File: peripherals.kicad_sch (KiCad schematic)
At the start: 36 parts, among them J10 SM04B-SRSS-TB, J11 U254-051T-4BH81-S2S, J3 UEXT, J8 XKTF-0803-0, Q1 BSS138, SW2 PROG_EN, U3 CH340C, U4 PCF8563T, Y1 32kHz

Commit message: Put resistor before switch to avoid parasitic powering of the board
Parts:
- R1: value 4.7K -> 1K
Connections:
- net USBTX: now also R1.2; no longer U3.2 (TXD)
- net at D1.1 (K): now also SW2.3 (C); no longer R1.2
- net at R1.1: now also U3.2 (TXD); no longer SW2.3 (C)
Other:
- moved on the sheet: R1
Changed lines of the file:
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@@
+    (stroke (width 0) (type default))
+  )
+  (wire (pts (xy 75.565 37.465) (xy 67.945 37.465))
     (stroke (width 0) (type default))
   )
@@
     (stroke (width 0) (type default))
   )
-  (wire (pts (xy 81.915 37.465) (xy 67.945 37.465))
+  (wire (pts (xy 81.915 37.465) (xy 80.645 37.465))
     (stroke (width 0) (type default))
   )
@@
     (stroke (width 0) (type default))
   )
-  (wire (pts (xy 43.18 40.005) (xy 40.64 40.005))
-    (stroke (width 0) (type default))
-  )
   (wire (pts (xy 119.38 53.975) (xy 111.76 53.975))
     (stroke (width 0) (type default))
@@
     (stroke (width 0) (type default))
   )
-  (wire (pts (xy 57.785 40.005) (xy 48.26 40.005))
+  (wire (pts (xy 40.64 40.005) (xy 57.785 40.005))
     (stroke (width 0) (type default))
   )
@@
     )
   )
-  (symbol (lib_id "Device:R_Small") (at 45.72 40.005 270) (unit 1)
+  (symbol (lib_id "Device:R_Small") (at 78.105 37.465 270) (unit 1)
     (in_bom yes) (on_board yes) (dnp no)
-    (property "Reference" "R1" (at 43.815 35.56 90)
+    (property "Reference" "R1" (at 76.2 33.02 90)
       (effects (font (size 1.27 1.27)) (justify left))
     )
-    (property "Value" "4.7K" (at 43.815 38.1 90)
+    (property "Value" "1K" (at 76.2 35.56 90)
       (effects (font (size 1.27 1.27)) (justify left))
     )
-    (property "Footprint" "Resistor_SMD:R_0402_1005Metric" (at 45.72 40.005 0)
-      (effects (font (size 1.27 1.27)) hide)
-    )
-    (property "Datasheet" "~" (at 45.72 40.005 0)
-      (effects (font (size 1.27 1.27)) hide)
-    )
+    (property "Footprint" "Resistor_SMD:R_0402_1005Metric" (at 78.105 37.465 0)
+      (effects (font (size 1.27 1.27)) hide)
+    )
+    (property "Datasheet" "~" (at 78.105 37.465 0)
+      (effects (font (size 1.27 1.27)) hide)
+    )

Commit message: Final touches
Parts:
- BT1: now not fitted
- renumbered C9 to C8, C10 to C9, D1 to D2, J3 to J11, J10 to J12, J11 to J9, R10 to R2, R12 to R3, R13 to R4, R14 to R5, R11 to R6, SW2 to SW3

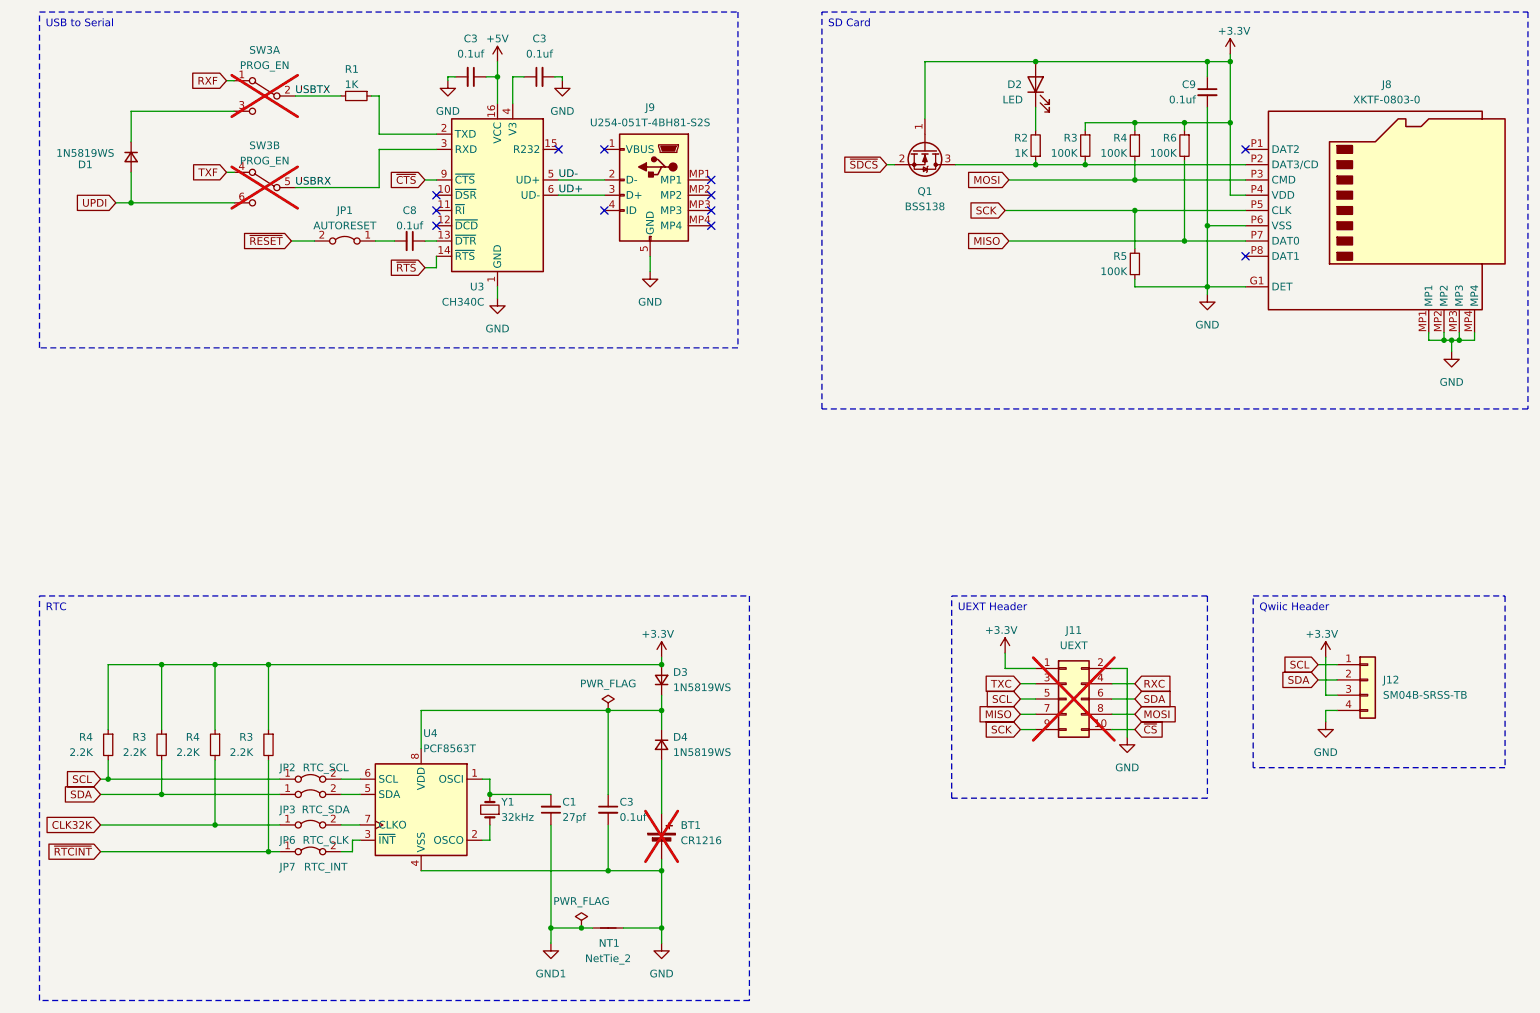
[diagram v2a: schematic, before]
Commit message: Switch to 4 layer; reduce connector size and move to edge
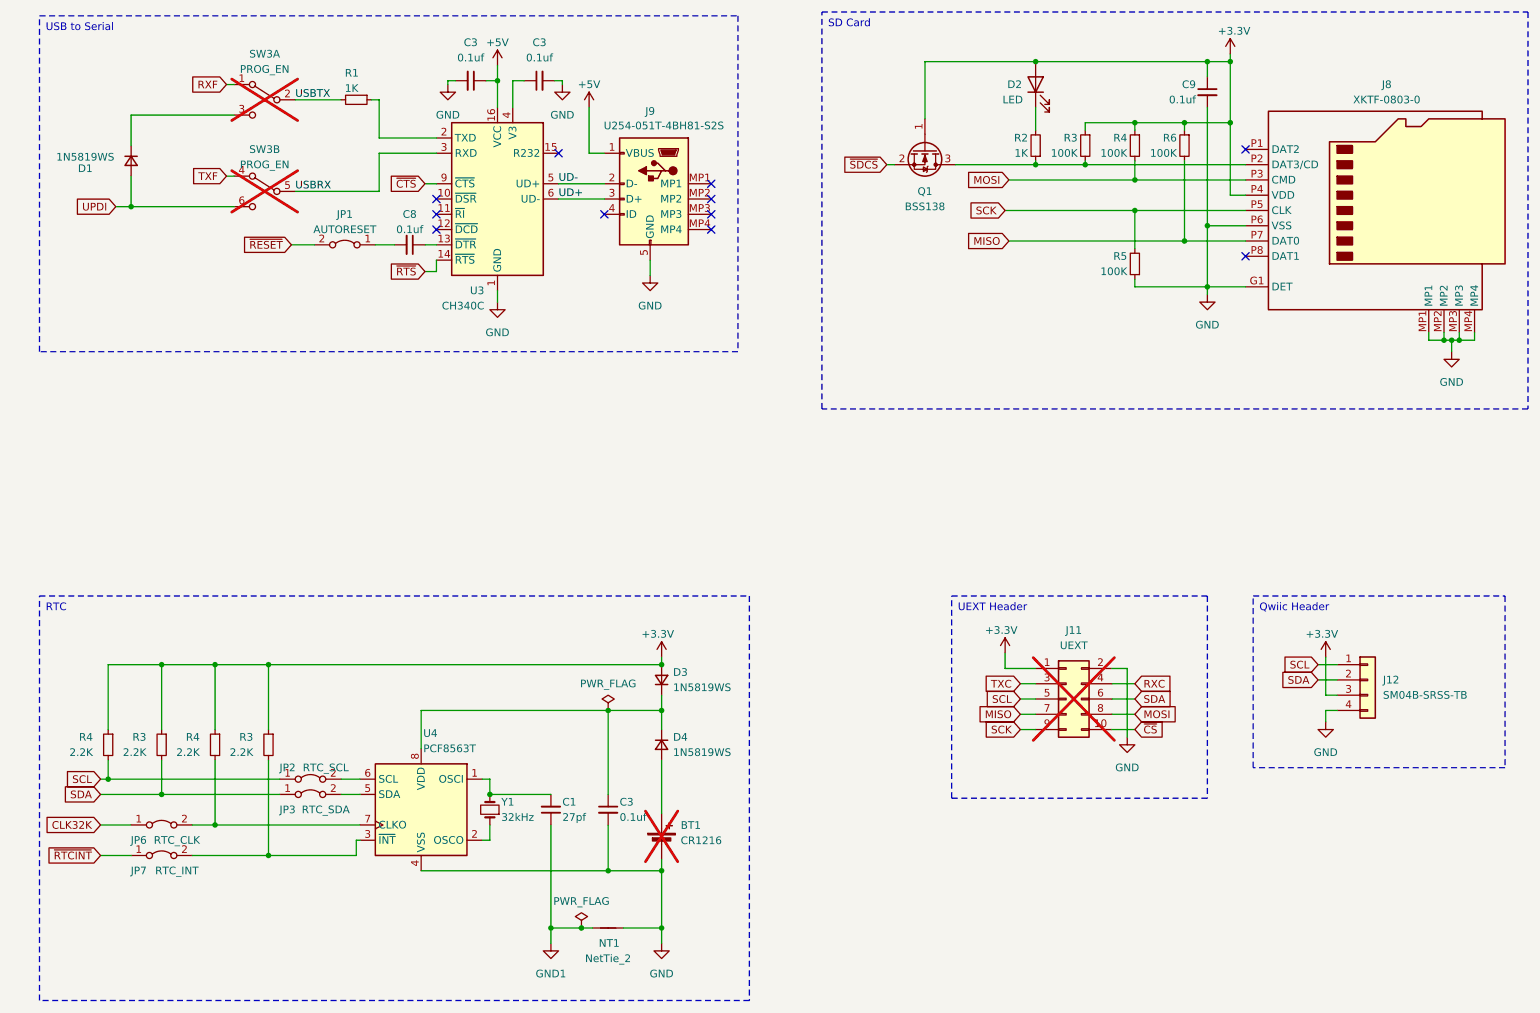
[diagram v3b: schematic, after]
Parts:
- JP6, JP7: footprint Jumper:SolderJumper-2_P1.3mm_Bridged_RoundedPad1.0x1.5mm -> Jumper:SolderJumper-2_P1.3mm_Open_RoundedPad1.0x1.5mm
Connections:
- net +5V: now also J9.1 (VBUS)
- net CLK32K: no longer R4.2
- net ~{RTCINT}: no longer R3.2
- net at JP7.2 (B), U4.3 (~{INT}): now also R3.2
- net at JP6.2 (B), U4.7 (CLKO): now also R4.2
- no-connect marks 12 -> 11
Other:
- moved on the sheet: C3, C8, D1, J9, JP1, JP6, JP7, R1, SW3A, SW3B, U3

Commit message: Add custom symbols and footprints
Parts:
- J12: footprint Custom:JST_SM04B-SRSS-TB_LF__SN_ -> SamacSys_Parts:SM04B-SRSS-TB_LFSN_
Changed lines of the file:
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@@
 			)
 		)
-		(property "Footprint" "Custom:JST_SM04B-SRSS-TB_LF__SN_"
+		(property "Footprint" "SamacSys_Parts:SM04B-SRSS-TB_LFSN_"
 			(at 246.38 134.62 0)
 			(effects
